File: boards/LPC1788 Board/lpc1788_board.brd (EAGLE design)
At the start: 257.2 x 187 mm, 90 parts, among them J1 5VDC, J10 MOLEX_527930570_5PIN_FFC_CONN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, J11 20PIN_10X2_.100IN, J12 DF12B-50DX_25X2_0.5MM, J2 SAMTEC_MUSB, J3 JST_2MM_SMT, J4 Console, J5 SMA-J-P-X-ST-EM1, J6 JTAG, J7 JTAG, J8 NHD-4.3-480272EF, J9 DF12B-50DX_25X2_0.5MM, Q1 MMBT2907, SW1 Reset, U1 LTC3127EMSEPBF, U2 MAX1551EZK+T, U3 LT3497EDDBTRMPBF, U4 CY62167_16MBIT_SRAM, U5 S25FL064P, Y1 12MHz

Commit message: more lpc1788 board changes
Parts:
- added R9: 10K, rcl:R0402
- moved J12 62.2 mm to (-89.1, 51.6), flipped to the bottom, turned to 270 degrees
- moved R8 58.8 mm to (26.7, 74.9), turned to 0 degrees
- moved J9 21.9 mm to (6.75, 110.9), flipped to the bottom
- moved R23 15.5 mm to (-37.3, 51.6)
- moved R24 15.5 mm to (-35.8, 51.6)
- moved R26 15.5 mm to (-33.3, 51.6)
- moved J6 15.5 mm to (-34.7, 49.8)
- moved R25 15.5 mm to (-34.5, 51.6)
- moved R13 12.9 mm to (-28.2, 46.7), flipped to the bottom
- moved R12 12.9 mm to (-25.7, 46.7), flipped to the bottom
- moved J11 12.5 mm to (-24.4, 41.0)
- moved R21 11.7 mm to (-15.5, 46.7)
- moved J8 10.6 mm to (6.50, 102.7)
- moved R22 4.93 mm to (-33.8, 105.2)
- moved R28 4.93 mm to (-29.7, 97.0)
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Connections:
- new net !CAS: J12.P$48, U$1.87
- new net !DYCS0: J12.P$39, U$1.73
- new net !RAS: J12.P$49, U$1.95
- new net CKE: J12.P$43, U$1.53
- new net CLK: J12.P$41, U$1.59
- new net DQM0: J12.P$45, U$1.49
- new net DQM1: J12.P$47, U$1.43
- net !BLS0: now also J12.P$44
- net !BLS1: now also J12.P$46
- net !CS1: now also J12.P$42
- net !OE: now also J12.P$35
- net !WE: now also J12.P$37
- net +3V3: no longer J12.P$2
- net +VBAT: now also R8.2
- net A0: now also J12.P$2
- net A1: now also J12.P$4
- net A10: now also J12.P$22
- net A11: now also J12.P$24
- net A12: now also J12.P$26
- net A13: now also J12.P$28
- net A14: now also J12.P$30
- net A15: now also J12.P$32
- net A16: now also J12.P$34
- net A17: now also J12.P$36
- net A18: now also J12.P$38
- net A19: now also J12.P$40
- net A2: now also J12.P$6
- net A3: now also J12.P$8
- net A4: now also J12.P$10
- net A5: now also J12.P$12
- net A6: now also J12.P$14
- net A7: now also J12.P$16
- net A8: now also J12.P$18
- net A9: now also J12.P$20
- net B0: now also J9.P$9
- net B1: now also J9.P$11
- net B2: now also J9.P$13
- net B3: now also J9.P$15
- net B4: now also J9.P$17
- net B5: now also J9.P$19
- net B6: now also J9.P$21
- net B7: now also J9.P$23
- net D0: now also J12.P$3
- net D1: now also J12.P$5
- net D10: now also J12.P$23
- net D11: now also J12.P$25
- net D12: now also J12.P$27
- net D13: now also J12.P$29
- net D14: now also J12.P$31
- net D15: now also J12.P$33
- net D2: now also J12.P$7
- net D3: now also J12.P$9
- net D4: now also J12.P$11
- net D5: now also J12.P$13
- net D6: now also J12.P$15
- net D7: now also J12.P$17
- net D8: now also J12.P$19
- net D9: now also J12.P$21
- net G0: now also J9.P$10
- net G1: now also J9.P$12
- net G2: now also J9.P$14
- net G3: now also J9.P$16
- net G4: now also J9.P$18
- net G5: now also J9.P$20
- net G6: now also J9.P$22
- net G7: now also J9.P$24
- net GND: now also R9.1; no longer J12.P$49
- net LCD_DCLK: now also J9.P$5
- net LCD_ENAB_M: now also J9.P$7
- net LCD_FP: now also J9.P$8
- net LCD_LE: now also J9.P$4
- net LCD_LP: now also J9.P$6
- net LCD_PWR: now also J9.P$3
- net LED1_PWR: now also J9.P$26
- net LED2_PWR: now also J9.P$28
- net LED_CTRL: now also R8.1, R9.2
- net R0: now also J9.P$25
- net R1: now also J9.P$27
- net R2: now also J9.P$29
- net R3: now also J9.P$31
- net R4: now also J9.P$33
- net R5: now also J9.P$35
- net R6: now also J9.P$37
- net R7: now also J9.P$39
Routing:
- net LED1_PWR: track 3.05 -> 54.3 mm, vias 0 -> 1
- net G3: track 0.00 -> 50.2 mm, vias 0 -> 2
- net G1: track 0.00 -> 49.4 mm, vias 0 -> 2
- net B0: track 0.00 -> 48.6 mm, vias 0 -> 2
- net G2: track 0.00 -> 48.2 mm, vias 0 -> 2
- net B1: track 0.00 -> 47.7 mm, vias 0 -> 2
- net G0: track 0.00 -> 45.6 mm, vias 0 -> 2
- net R1: track 0.00 -> 45.2 mm, vias 0 -> 4
- net R0: track 0.00 -> 44.1 mm, vias 0 -> 4
- net LCD_PWR: track 0.00 -> 43.8 mm, vias 0 -> 2
- net LCD_DCLK: track 0.00 -> 39.1 mm, vias 0 -> 2
- net LCD_FP: track 0.00 -> 38.6 mm, vias 0 -> 2
- net LCD_ENAB_M: track 0.00 -> 38.4 mm, vias 0 -> 2
- net LCD_LP: track 0.00 -> 36.5 mm, vias 0 -> 2
- net R5: track 0.00 -> 27.2 mm, vias 0 -> 2
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
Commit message: more layout of LPC1788 board
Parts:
- removed J7: JTAG, Custom:8-PIN_SIP_.100IN
- removed R21: 0, rcl:R0603
- added SW2: OS102011MA1QS1, Custom:OS102011MA1QS1
- moved J12 51.2 mm to (-41.9, 71.2)
- moved R30 49.8 mm to (22.2, 84.2), turned to 270 degrees
- moved J10 49.6 mm to (29.8, 79.9), flipped to the bottom, turned to 90 degrees
- moved R29 44.7 mm to (22.2, 79.5)
- moved R13 31.8 mm to (1.06, 59.3)
- moved R12 28.1 mm to (-0.53, 59.3)
- moved J9 25.0 mm to (-16.7, 102.1), flipped to the top, turned to 0 degrees
- moved R22 20.3 mm to (-44.3, 87.8), turned to 270 degrees
- moved R14 16.9 mm to (20.1, 91.5)
- moved R20 14.3 mm to (-40.3, 58.2), turned to 0 degrees
- moved J4 13.3 mm to (26.0, 81.2)
- moved C16 13.3 mm to (-7.91, 41.5), turned to 0 degrees
- moved SW1 11.9 mm to (-5.60, 42.6)
- moved U5 11.5 mm to (-39.8, 92.5), turned to 180 degrees
- moved R11 11.1 mm to (-3.45, 41.5), turned to 180 degrees
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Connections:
- removed net N$36: J7.1, R21.1
- new net N$20: J3.2, SW2.P$2
- net +3V3: no longer R21.2
- net +VBAT: now also SW2.P$3; no longer J3.2
- net /RESET: no longer J7.6
- net GND: no longer J7.8
- net KEY_I2C_SCL: now also U$1.141; no longer U$1.48
- net KEY_I2C_SDA: now also U$1.117; no longer U$1.50
- net SCL: now also R12.2, U$1.48; no longer R13.2, U$1.141
- net SDA: now also R13.2, U$1.50; no longer R12.2, U$1.117
- net TCK/SWDCLK: no longer J7.3
- net TDI: no longer J7.5
- net TDO/SWO: no longer J7.4
- net TMS/SWDIO: no longer J7.2
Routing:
- net SPI_SCK: track 0.00 -> 59.9 mm, vias 0 -> 1
- net SPI_MOSI: track 0.00 -> 58.7 mm, vias 0 -> 1
- net A3: track 0.00 -> 58.0 mm, vias 0 -> 2
- net A16: track 0.00 -> 57.8 mm, vias 0 -> 3
- net SPI_MISO: track 0.00 -> 57.7 mm, vias 0 -> 1
- net SPI_CS: track 0.00 -> 56.6 mm, vias 0 -> 1
- net SD_DAT_2: track 0.00 -> 56.5 mm, vias 0 -> 4
- net EXT_UART_RX: track 0.00 -> 55.9 mm, vias 0 -> 1
- net EXT_UART_TX: track 0.00 -> 55.7 mm, vias 0 -> 1
- net SD_DAT_3: track 0.00 -> 55.0 mm, vias 0 -> 2
- net A0: track 0.00 -> 54.7 mm, vias 0 -> 2
- net A1: track 0.00 -> 53.9 mm, vias 0 -> 2
- net A2: track 0.00 -> 53.6 mm, vias 0 -> 2
- net A5: track 2.60 -> 54.8 mm, vias 1 -> 2
- net LED1_PWR: track 54.3 -> 2.59 mm
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- added copper zone on layer 16, net +3V3
- added copper zone on layer 16, net N$20
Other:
- board size 257.2 x 187 mm -> 81.8 x 67.7 mm

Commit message: Finishing up LCP1788 board
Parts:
- added C33, C34: 0.01uF, rcl:C0402
- added C35: 0.1uF, rcl:C0402
- added C36: 10uF, rcl:C0402
- added C37: 330uF, rcl:C1206
- added R10, R21, R31: 20K, rcl:R0402
- added U6: AR1021-RESISTIVE_TOUCH_CONTROLLER, Custom:SSOP-20
- moved J10 64.1 mm to (-31.1, 99.8), turned to 0 degrees
- moved R29 56.1 mm to (-30.0, 100.2), flipped to the top, turned to 270 degrees
- moved R30 55.8 mm to (-31.3, 100.2), flipped to the top
- moved R14 10.5 mm to (16.5, 81.6), turned to 90 degrees
- moved R20 8.17 mm to (-32.2, 59.4), flipped to the top, turned to 180 degrees
- moved J8 4.88 mm to (11.4, 100.9)
- moved J12 3.36 mm to (-38.6, 71.4)
- moved Q1 1.52 mm to (9.27, 55.4)
- moved R13 1.02 mm to (0.61, 60.2)
- moved R12 1.00 mm to (-0.98, 60.2)
- moved J9 0.76 mm to (-16.7, 101.3)
- moved J2 0.61 mm to (11.1, 39.4)
- moved J5 0.61 mm to (-45.3, 53.0)
- moved R19 0.31 mm to (-38.3, 84.0), flipped to the top
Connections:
- new net N$35: C33.1, J8.P$39, R10.2, U6.P$19
- new net N$36: J8.P$37, U6.P$18
- new net N$37: C34.1, J8.P$38, U6.P$16
- new net N$38: J8.P$40, U6.P$15
- new net N$39: R21.2, U6.P$2
- new net N$40: R10.1, U6.P$5
- new net N$41: R31.2, U6.P$4
- new net TOUCH_INT: U$1.91, U6.P$9
- net !BLS0: now also J12.P$3; no longer J12.P$44
- net !BLS1: now also J12.P$20; no longer J12.P$46
- net !CAS: now also J12.P$21; no longer J12.P$48
- net !CS1: now also J12.P$33; no longer J12.P$42
- net !DYCS0: now also J12.P$31; no longer J12.P$39
- net !OE: now also J12.P$29; no longer J12.P$35
- net !RAS: now also J12.P$19; no longer J12.P$49
- net !WE: now also J12.P$2; no longer J12.P$37
- net +3V3: now also C35.1, C36.1, J9.P$3, J9.P$4, U6.P$1
- net +VBAT: now also C37.1
- net A0: now also J12.P$27; no longer J12.P$2
- net A1: now also J12.P$25; no longer J12.P$4
- net A10: now also J12.P$14; no longer J12.P$22
- net A11: now also J12.P$12; no longer J12.P$24
- net A12: now also J12.P$10; no longer J12.P$26
- net A13: now also J12.P$22; no longer J12.P$28
- net A14: now also J12.P$8; no longer J12.P$30
- net A15: now also J12.P$6; no longer J12.P$32
- net A16: now also J12.P$48; no longer J12.P$34
- net A17: now also J12.P$13; no longer J12.P$36
- net A18: now also J12.P$11; no longer J12.P$38
- net A19: now also J12.P$7; no longer J12.P$40
- net A2: now also J12.P$23; no longer J12.P$6
- net A3: now also J12.P$17; no longer J12.P$8
- net A4: now also J12.P$15; no longer J12.P$10
- net A5: now also J12.P$9; no longer J12.P$12
- net A6: now also J12.P$5; no longer J12.P$14
- net A7: now also J12.P$4; no longer J12.P$16
- net A9: now also J12.P$16; no longer J12.P$20
- net B0: now also J9.P$11; no longer J9.P$9
- net B1: now also J9.P$13; no longer J9.P$11
- net B2: now also J9.P$8; no longer J9.P$13
- net B3: now also J9.P$6; no longer J9.P$15
- net B4: now also J9.P$37; no longer J9.P$17
- net B5: now also J9.P$39; no longer J9.P$19
- net B6: now also J9.P$41; no longer J9.P$21
- net B7: now also J9.P$43; no longer J9.P$23
- net CKE: now also J12.P$44; no longer J12.P$43
- net CLK: now also J12.P$46; no longer J12.P$41
- net D0: now also J12.P$37; no longer J12.P$3
- net D1: now also J12.P$39; no longer J12.P$5
- net D10: now also J12.P$45; no longer J12.P$23
- net D11: now also J12.P$49; no longer J12.P$25
- net D12: now also J12.P$28; no longer J12.P$27
- net D13: now also J12.P$32; no longer J12.P$29
- net D14: now also J12.P$36; no longer J12.P$31
- net D15: now also J12.P$40; no longer J12.P$33
- net D2: now also J12.P$43; no longer J12.P$7
- net D3: now also J12.P$47; no longer J12.P$9
- net D4: now also J12.P$26; no longer J12.P$11
- net D5: now also J12.P$30; no longer J12.P$13
- net D6: now also J12.P$34; no longer J12.P$15
- net D7: now also J12.P$38; no longer J12.P$17
- net D8: now also J12.P$35; no longer J12.P$19
- net D9: now also J12.P$41; no longer J12.P$21
- net DQM0: now also J12.P$42; no longer J12.P$45
- net DQM1: now also J12.P$24; no longer J12.P$47
- net G0: now also J9.P$15; no longer J9.P$10
- net G1: now also J9.P$5; no longer J9.P$12
- net G2: now also J9.P$22; no longer J9.P$14
- net G3: now also J9.P$24; no longer J9.P$16
- net G4: now also J9.P$16; no longer J9.P$18
- net G5: now also J9.P$14; no longer J9.P$20
- net G6: now also J9.P$12; no longer J9.P$22
- net G7: now also J9.P$10; no longer J9.P$24
- net GND: now also C33.2, C34.2, C35.2, C36.2, C37.2, J9.P$47, J9.P$48, R21.1, R31.1, U6.P$20
- net LCD_DCLK: now also J9.P$21; no longer J9.P$5
- net LCD_ENAB_M: now also J9.P$25; no longer J9.P$7
- net LCD_FP: now also J9.P$23; no longer J9.P$8
- net LCD_LE: now also J9.P$19; no longer J9.P$4
- net LCD_LP: now also J9.P$27; no longer J9.P$6
- net LCD_PWR: now also J9.P$17; no longer J9.P$3
- net LED1_PWR: now also J9.P$30, J9.P$32; no longer J9.P$26
- net LED2_PWR: now also J9.P$36, J9.P$38; no longer J9.P$28
- net R0: now also J9.P$9; no longer J9.P$25
- net R1: now also J9.P$7; no longer J9.P$27
- net R2: now also J9.P$33; no longer J9.P$29
- net R3: now also J9.P$35; no longer J9.P$31
- net R4: now also J9.P$29; no longer J9.P$33
- net R5: now also J9.P$31; no longer J9.P$35
- net R6: now also J9.P$18; no longer J9.P$37
- net R7: now also J9.P$20; no longer J9.P$39
- net SCL: now also U6.P$11
- net SDA: now also U6.P$13
- net SD_DET: now also U$1.99
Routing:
- net +3V3: track 295.4 -> 483.1 mm, vias 25 -> 32
- net KEY_INT: track 12.9 -> 113.5 mm, vias 1 -> 3
- net LED1_PWR: track 2.59 -> 76.5 mm, vias 1 -> 5
- net LED2_PWR: track 2.65 -> 73.9 mm, vias 1 -> 4
- net GND: track 29.0 -> 90.6 mm, vias 21 -> 81
- net SCL: track 37.6 -> 87.5 mm, vias 1 -> 2
- net SDA: track 42.4 -> 92.0 mm, vias 2 -> 3
- net B2: track 16.5 -> 63.2 mm
- net B3: track 18.8 -> 62.6 mm, vias 1 -> 0
- net KEY_I2C_SDA: track 0.00 -> 43.5 mm, vias 0 -> 4
- net B4: track 34.9 -> 77.1 mm, vias 2 -> 3
- net B6: track 31.7 -> 72.9 mm, vias 2 -> 3
- net B5: track 34.0 -> 73.6 mm
- net B7: track 32.8 -> 71.4 mm
- net G2: track 46.4 -> 84.6 mm, vias 2 -> 4
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- added copper zone on layer 16, net +VBAT
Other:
- board text added: "ADD GND PLANE VIAS"
- board text added: "Ryan Mamonw 2014"

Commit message: updates
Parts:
- moved J5 2.30 mm to (-47.6, 53.0)
- moved J2 1.40 mm to (11.1, 38.0)
- moved J1 1.30 mm to (23.9, 47.6)
- moved J3 1.00 mm to (30.0, 62.4)
- moved SW2 1.00 mm to (34.8, 52.3)
- moved U$3 1.00 mm to (27.1, 91.9)
- moved R22 0.63 mm to (-43.6, 87.9)
- moved R28 0.63 mm to (-35.4, 97.9)
- moved U5 0.63 mm to (-39.2, 92.6)
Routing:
- net +VUSB: track 34.2 -> 37.0 mm
- net N$27: track 28.0 -> 30.3 mm
- net N$20: track 6.42 -> 8.42 mm
- net D_P: track 8.08 -> 9.48 mm
- net D_N: track 10.0 -> 11.4 mm
- net V+: track 8.04 -> 9.34 mm
- net SD_DAT_3: track 53.6 -> 54.6 mm
- net SD_DAT_2: track 52.3 -> 53.3 mm
- net SD_DAT_0: track 26.3 -> 27.3 mm
- net SD_CMD: track 28.6 -> 29.6 mm
- net SD_CLK: track 28.8 -> 29.8 mm
- net +VBAT: track 55.4 -> 56.4 mm
- net SD_DAT_1: track 46.1 -> 47.1 mm
- net SPI_FLASH_MOSI: track 33.8 -> 33.1 mm
- net SD_DET: track 27.8 -> 28.4 mm
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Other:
- board size 81.8 x 67.7 mm -> 85 x 70 mm
- board text added: "Ryan Mamone 2014"
- board text removed: "Ryan Mamonw 2014"

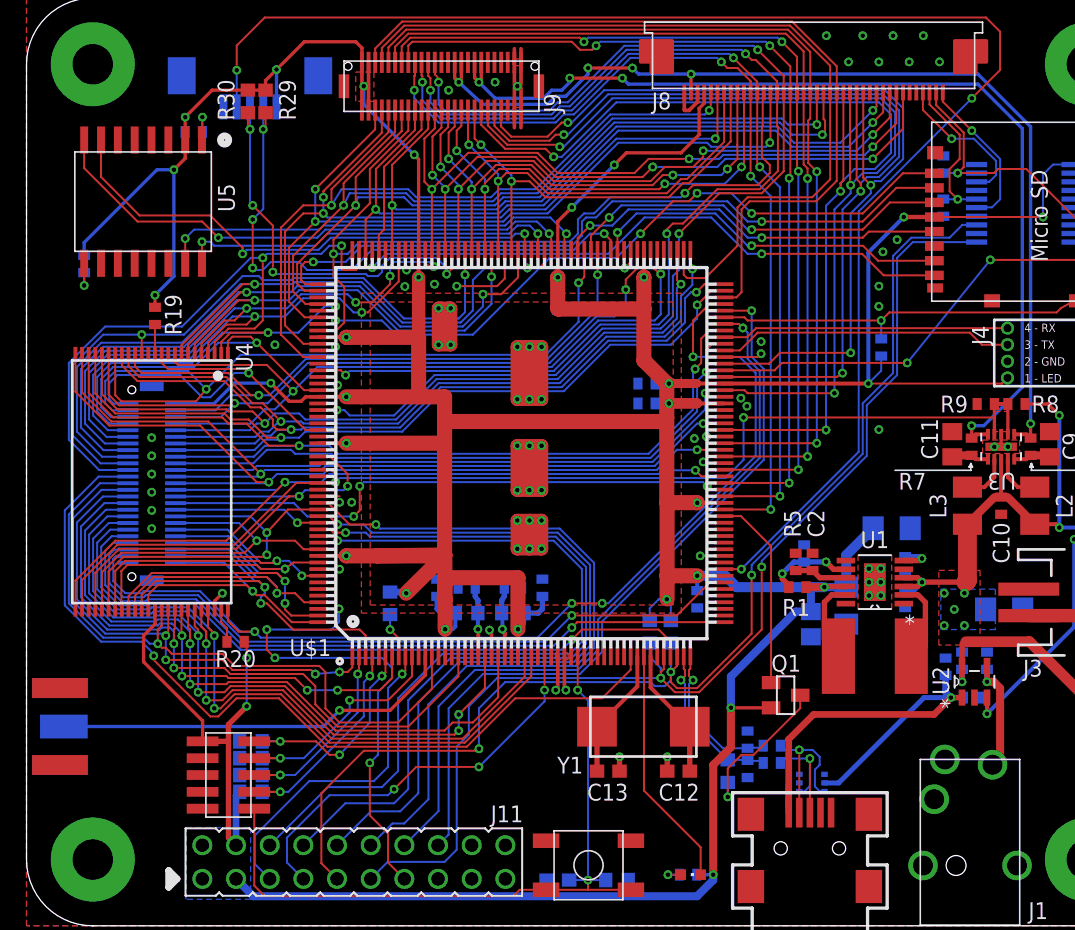
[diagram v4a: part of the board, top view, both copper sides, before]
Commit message: switch to sdram
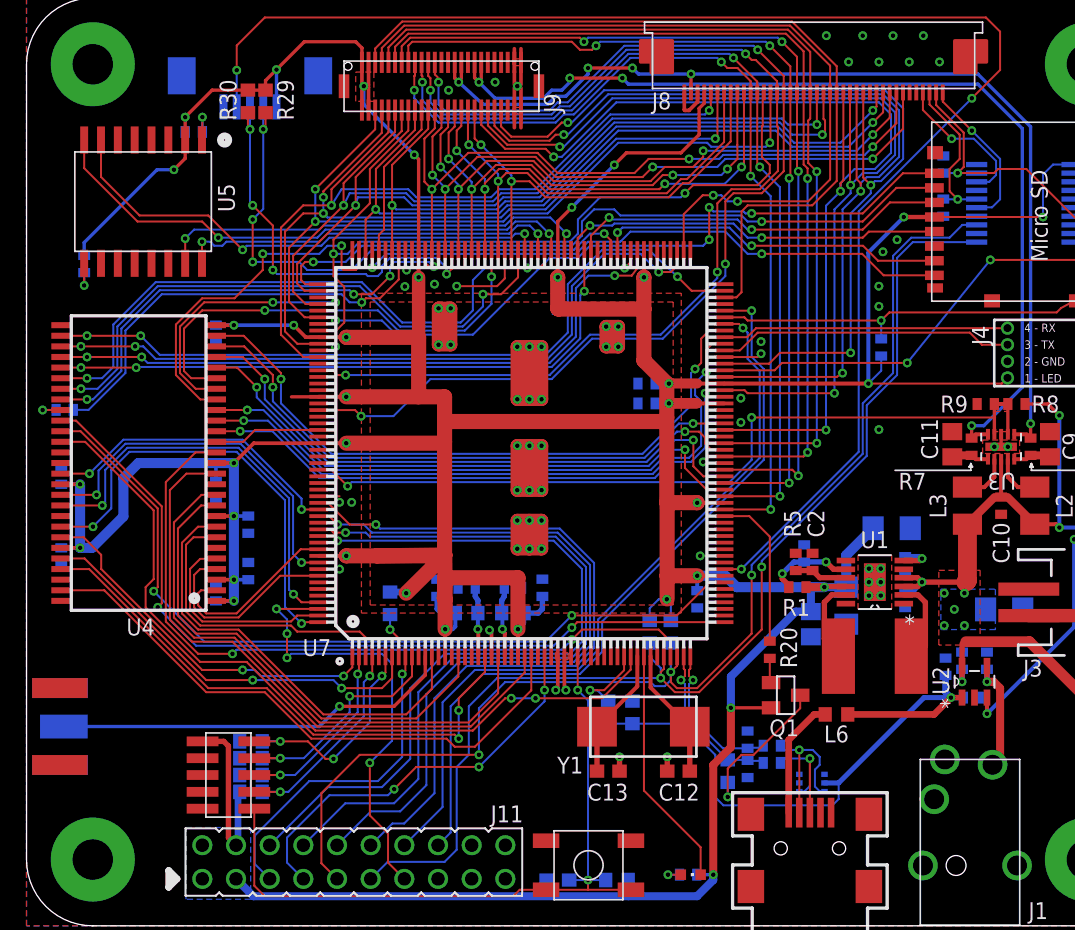
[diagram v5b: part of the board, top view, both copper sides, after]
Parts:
- removed J12: DF12B-50DX_25X2_0.5MM, Custom:DF12B-50DX_25X2_0.5MM
- added C38, C39, C40, C41, C42, C43, C44: 0.1uF, rcl:C0402
- added L6: 470nH, Custom:0603
- added R32: 24K, rcl:R0603
- added R33: 39K, rcl:R0603
- R19: value 10k -> 0
- R20: value 10k -> 22
- U4: value CY62167_16MBIT_SRAM -> AS4C8M16S-128MBIT_SDRAM; device Custom:TSOP48 -> Custom:TSOP54-II
- moved R20 40.3 mm to (8.08, 58.8), turned to 270 degrees
- moved R19 9.83 mm to (-45.1, 76.9), flipped to the bottom, turned to 0 degrees
- moved U4 1.72 mm to (-39.5, 72.9), turned to 180 degrees
- renumbered U$1 to U7, U$4 to U8
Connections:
- removed net !BLS0: J12.P$3, U4.15, U7.119
- removed net !BLS1: J12.P$20, U4.14, U7.139
- removed net !CS0: U4.26, U7.187
- removed net !CS1: J12.P$33, U7.193
- removed net !OE: J12.P$29, U4.28, U7.183
- removed net A15: J12.P$6, U4.1, U7.173
- removed net A16: J12.P$48, U4.48, U7.101
- removed net A17: J12.P$13, U4.17, U7.104
- removed net A18: J12.P$11, U4.16, U7.105
- removed net A19: J12.P$7, U4.9, U7.111
- new net N$42: R32.2, U7.42
- new net N$43: J2.1, L6.1
- net !CAS: now also U4.P$17; no longer J12.P$21
- net !DYCS0: now also U4.P$19; no longer J12.P$31
- net !RAS: now also U4.P$18; no longer J12.P$19
- net !WE: now also U4.P$16; no longer J12.P$2, U4.11
- net +3V3: now also C38.1, C39.1, C40.1, C41.1, C42.1, C43.1, C44.1, U4.P$1, U4.P$14, U4.P$27, U4.P$3, U4.P$43, U4.P$49, U4.P$9; no longer J12.P$1, R19.1, R20.1, U4.37
- net +VUSB: now also L6.2, R32.1, R33.1; no longer J2.1
- net A0: now also U4.P$23; no longer J12.P$27, U4.25
- net A1: now also U4.P$24; no longer J12.P$25, U4.24
- net A10: now also U4.P$22; no longer J12.P$14, U4.6
- net A11: now also U4.P$35; no longer J12.P$12, U4.5
- net A12: now also R19.1; no longer J12.P$10, U4.4
- net A13: now also U4.P$20; no longer J12.P$22, U4.3
- net A14: now also U4.P$21; no longer J12.P$8, U4.2
- net A2: now also U4.P$25; no longer J12.P$23, U4.23
- net A3: now also U4.P$26; no longer J12.P$17, U4.22
- net A4: now also U4.P$29; no longer J12.P$15, U4.21
- net A5: now also U4.P$30; no longer J12.P$9, U4.20
- net A6: now also U4.P$31; no longer J12.P$5, U4.19
- net A7: now also U4.P$32; no longer J12.P$4, U4.18
- net A8: now also U4.P$33; no longer J12.P$18, U4.8
- net A9: now also U4.P$34; no longer J12.P$16, U4.7
- net CKE: now also U4.P$37; no longer J12.P$44
- net CLK: now also U4.P$38; no longer J12.P$46
- net D0: now also U4.P$2; no longer J12.P$37, U4.29
- net D1: now also U4.P$4; no longer J12.P$39, U4.31
- net D10: now also U4.P$45; no longer J12.P$45, U4.34
- net D11: now also U4.P$47; no longer J12.P$49, U4.36
- net D12: now also U4.P$48; no longer J12.P$28, U4.39
- net D13: now also U4.P$50; no longer J12.P$32, U4.41
- net D14: now also U4.P$51; no longer J12.P$36, U4.43
- net D15: now also U4.P$53; no longer J12.P$40, U4.45
- net D2: now also U4.P$5; no longer J12.P$43, U4.33
- net D3: now also U4.P$7; no longer J12.P$47, U4.35
- net D4: now also U4.P$8; no longer J12.P$26, U4.38
- net D5: now also U4.P$10; no longer J12.P$30, U4.40
- net D6: now also U4.P$11; no longer J12.P$34, U4.42
- net D7: now also U4.P$13; no longer J12.P$38, U4.44
- net D8: now also U4.P$42; no longer J12.P$35, U4.30
- net D9: now also U4.P$44; no longer J12.P$41, U4.32
- net DQM0: now also U4.P$15; no longer J12.P$42
- net DQM1: now also U4.P$39; no longer J12.P$24
- net GND: now also C38.2, C39.2, C40.2, C41.2, C42.2, C43.2, C44.2, R33.2, U4.P$12, U4.P$28, U4.P$41, U4.P$46, U4.P$52, U4.P$54, U4.P$6; no longer J12.P$50, U4.27, U4.46
- net N$22: now also R20.1; no longer Q1.1
- net N$28: now also U4.P$36; no longer U4.12
- net N$29: now also Q1.1; no longer U4.47
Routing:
- net A16: track 79.2 -> 0.00 mm, vias 4 -> 0
- net A17: track 63.3 -> 0.00 mm, vias 2 -> 0
- net A18: track 61.7 -> 0.00 mm, vias 2 -> 0
- net A19: track 55.6 -> 0.00 mm, vias 2 -> 0
- net !BLS0: track 50.6 -> 0.00 mm, vias 2 -> 0
- net !BLS1: track 50.5 -> 0.00 mm, vias 2 -> 0
- net !OE: track 37.5 -> 0.00 mm, vias 2 -> 0
- net A15: track 27.0 -> 0.00 mm, vias 1 -> 0
- net !CS0: track 23.1 -> 0.00 mm
- net A13: track 49.7 -> 27.7 mm
- net +3V3: track 482.8 -> 504.7 mm, vias 32 -> 36
- net !WE: track 29.6 -> 8.11 mm, vias 1 -> 0
- net A3: track 69.0 -> 49.7 mm
- net A10: track 53.8 -> 35.1 mm
- net A1: track 62.7 -> 44.3 mm
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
